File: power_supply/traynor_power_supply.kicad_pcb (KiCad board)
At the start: 2 copper layers, 117 x 47.5 mm, 34 parts, among them J1 AC IN, J10 OUT2, J11 OUT3, J2 AC IN, J3 Chassis GND, J4 OUT1, J5 TREM, J6 SW, J7 SW, J8 CHOKE, J9 CHOKE

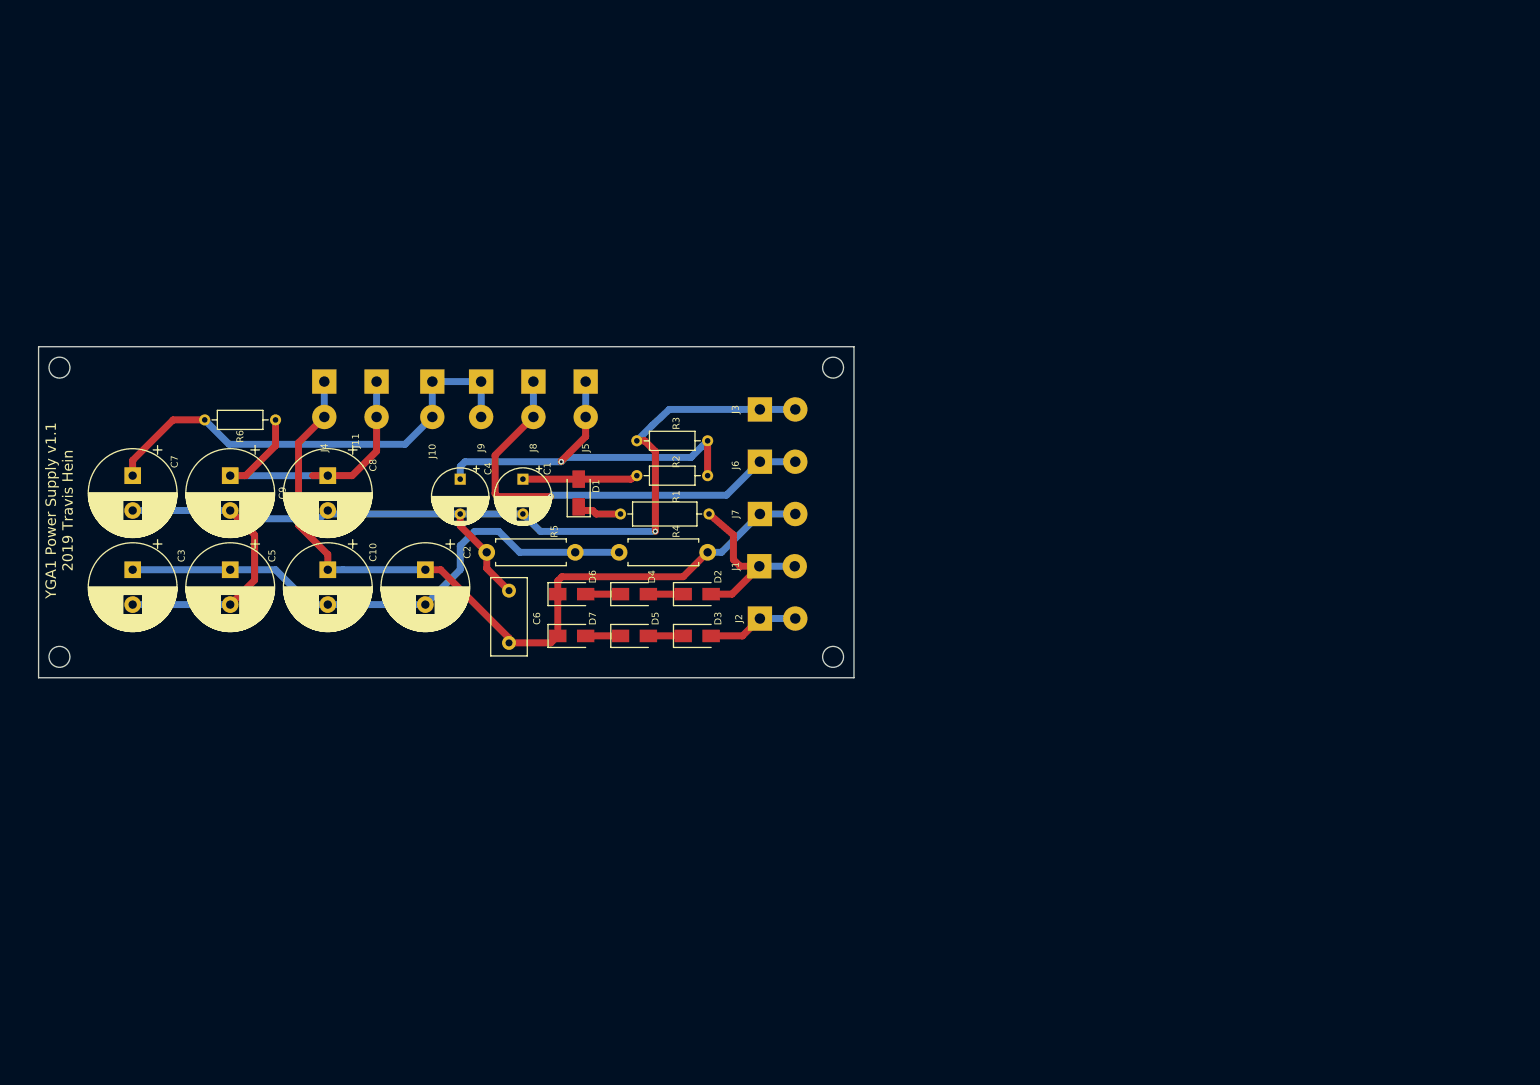
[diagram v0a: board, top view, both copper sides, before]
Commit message: power supply module
assemble circuit board after it arrived.
update schematic to fix bugs and small improvements we observed while wiring it up.
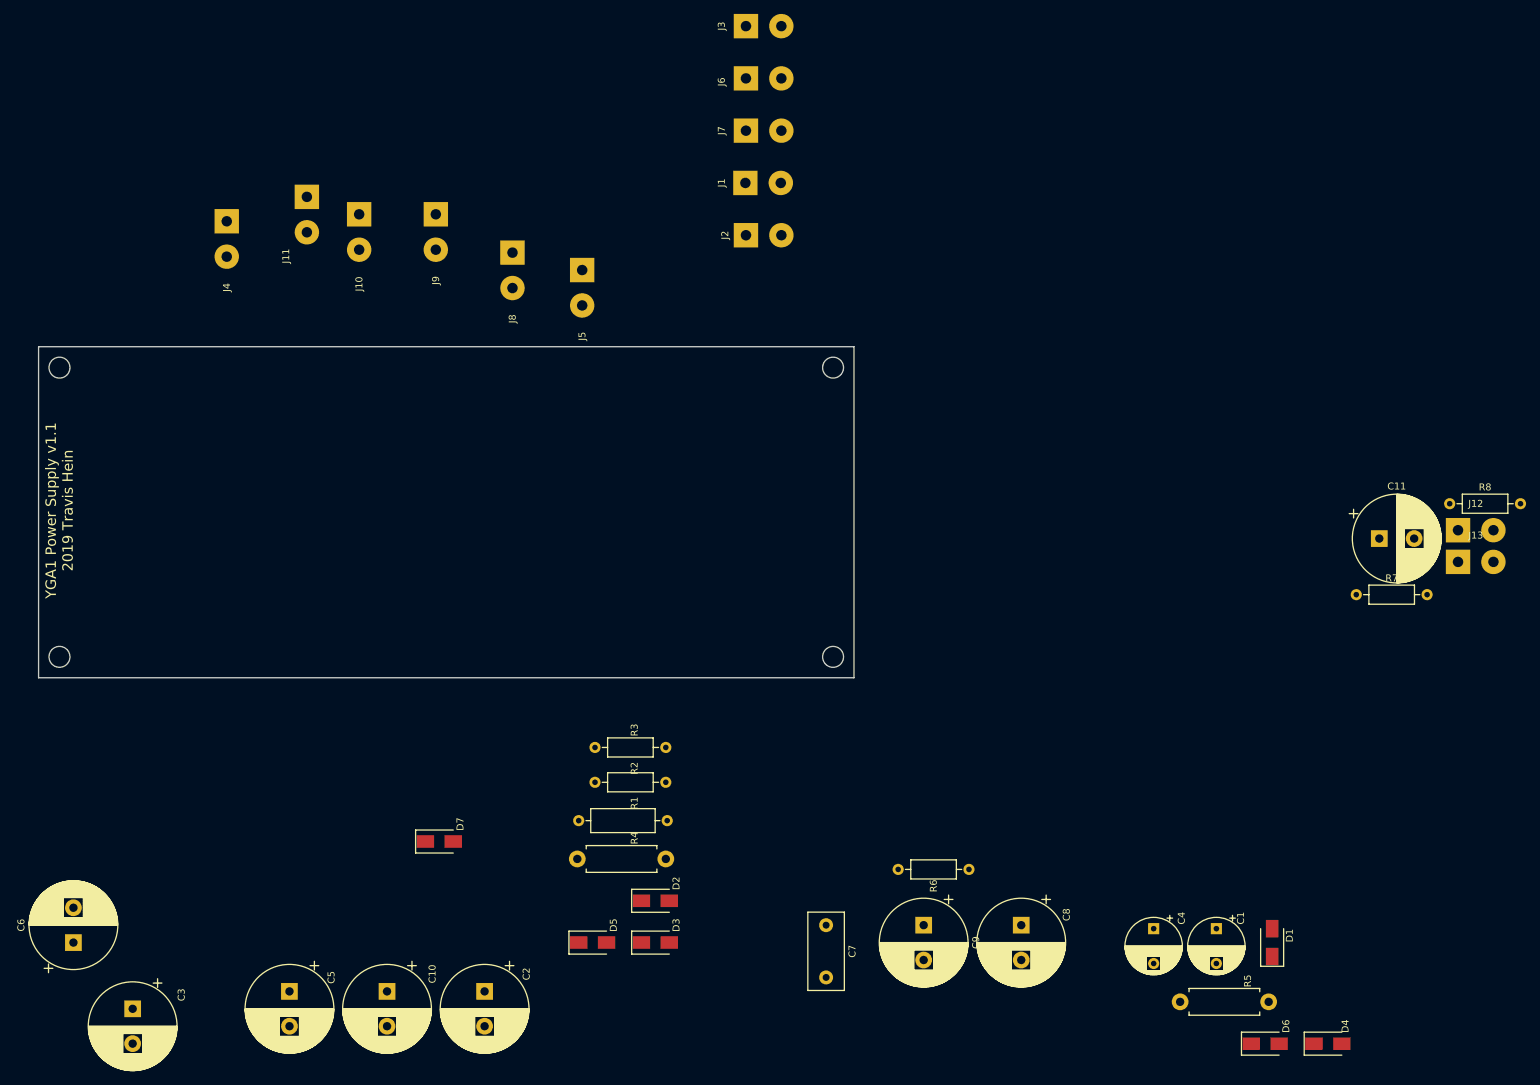
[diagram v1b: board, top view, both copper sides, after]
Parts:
- added C11: 47uF 450V, Capacitor_THT:CP_Radial_D12.5mm_P5.00mm, F.Cu at (242.4, 110.0)
- added J12: +340V, Connector_Wire:SolderWirePad_1x02_P5.08mm_Drill1.5mm, F.Cu at (253.7, 108.8)
- added J13: +340V, Connector_Wire:SolderWirePad_1x02_P5.08mm_Drill1.5mm, F.Cu at (253.7, 113.4)
- added R7: 4.70 1W, Resistor_THT:R_Axial_DIN0207_L6.3mm_D2.5mm_P10.16mm_Horizontal, F.Cu at (239.1, 118.1)
- added R8: 4.7K 1W, Resistor_THT:R_Axial_DIN0207_L6.3mm_D2.5mm_P10.16mm_Horizontal, F.Cu at (252.5, 105.0)
- C6: value 0.047uF 600V -> 47uF 450V; footprint Capacitor_THT:C_Disc_D11.0mm_W5.0mm_P7.50mm -> Capacitor_THT:CP_Radial_D12.5mm_P5.00mm
- C7: value 47uF 450V -> 0.047uF 600V; footprint Capacitor_THT:CP_Radial_D12.5mm_P5.00mm -> Capacitor_THT:C_Disc_D11.0mm_W5.0mm_P7.50mm
- C9: value 10uF 450V -> 47uF 450V
- J10: value OUT2 -> +340V
- J11: value OUT3 -> +340V
- J4: value OUT1 -> -40V
- J5: value TREM -> SW
- J6: value SW -> CHOKE
- J7: value SW -> Audio_center_tap
- J8, J9: value CHOKE -> Output tube
- R6: value 4.7K 1W -> 4.70 1W
- moved C1 118.6 mm to (219.0, 166.0)
- moved C4 118.6 mm to (210.0, 166.0)
- moved C7 118.6 mm to (163.0, 165.5)
- moved C8 118.6 mm to (191.0, 165.5)
- moved C9 118.6 mm to (177.0, 165.5)
- moved D1 118.6 mm to (227.0, 168.0)
- moved D4 118.6 mm to (235.0, 182.5)
- moved D6 118.6 mm to (226.0, 182.5)
- moved R5 118.6 mm to (226.5, 176.5)
- moved R6 118.6 mm to (183.5, 157.5)
- moved C6 75.9 mm to (55.0, 168.0)
- moved C3 63.0 mm to (63.5, 177.5)
- moved C10 61.1 mm to (100.0, 175.0)
- moved C2 61.1 mm to (114.0, 175.0)
- moved C5 61.1 mm to (86.0, 175.0)
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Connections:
- C10 pad 2: Net-(C10-Pad2) -> Net-(C1-Pad1)
- C2 pad 1: Net-(C10-Pad1) -> Net-(C2-Pad1)
- C2 pad 2: Net-(C10-Pad2) -> Net-(C2-Pad2)
- C3 pad 1: Net-(C10-Pad2) -> Net-(C2-Pad2)
- C3 pad 2: Net-(C1-Pad2) -> Net-(C1-Pad1)
- C4 pad 1: Net-(C4-Pad1) -> Net-(C1-Pad1)
- C4 pad 2: Net-(C1-Pad2) -> Net-(C4-Pad2)
- C5 pad 1: Net-(C10-Pad2) -> Net-(C2-Pad1)
- C5 pad 2: Net-(C1-Pad2) -> Net-(C2-Pad2)
- C6 pad 1: Net-(C10-Pad1) -> Net-(C2-Pad2)
- C6 pad 2: Net-(C1-Pad2) -> Net-(C1-Pad1)
- C7 pad 1: Net-(C7-Pad1) -> Net-(C2-Pad1)
- C7 pad 2: Net-(C1-Pad2) -> Net-(C1-Pad1)
- C8 pad 2: Net-(C1-Pad2) -> Net-(C1-Pad1)
- C9 pad 2: Net-(C1-Pad2) -> Net-(C1-Pad1)
- D1 pad 2: Net-(C1-Pad1) -> Net-(C1-Pad2)
- D6 pad 1: Net-(C10-Pad1) -> Net-(C2-Pad1)
- D7 pad 1: Net-(C10-Pad1) -> Net-(C2-Pad1)
- J10 pad 1: Net-(C7-Pad1) -> Net-(C10-Pad1)
- J10 pad 2: Net-(C7-Pad1) -> Net-(C10-Pad1)
- J11 pad 1: Net-(C8-Pad1) -> Net-(C10-Pad1)
- J11 pad 2: Net-(C8-Pad1) -> Net-(C10-Pad1)
- J3 pad 1: Net-(C1-Pad2) -> Net-(C1-Pad1)
- J3 pad 2: Net-(C1-Pad2) -> Net-(C1-Pad1)
- J4 pad 1: Net-(C10-Pad1) -> Net-(C4-Pad2)
- J4 pad 2: Net-(C10-Pad1) -> Net-(C4-Pad2)
- J5 pad 1: Net-(C4-Pad1) -> Net-(C2-Pad1)
- J5 pad 2: Net-(C4-Pad1) -> Net-(C2-Pad1)
- J6 pad 1: Net-(J6-Pad1) -> Net-(C8-Pad1)
- J6 pad 2: Net-(J6-Pad1) -> Net-(C8-Pad1)
- J7 pad 1: Net-(C10-Pad1) -> Net-(C8-Pad1)
- J7 pad 2: Net-(C10-Pad1) -> Net-(C8-Pad1)
- J8 pad 1: Net-(J6-Pad1) -> Net-(J8-Pad1)
- J8 pad 2: Net-(J6-Pad1) -> Net-(J8-Pad1)
- J9 pad 1: Net-(C7-Pad1) -> Net-(J9-Pad1)
- J9 pad 2: Net-(C7-Pad1) -> Net-(J9-Pad1)
- R2 pad 1: Net-(C4-Pad1) -> Net-(C4-Pad2)
- R2 pad 2: Net-(C1-Pad1) -> Net-(C1-Pad2)
- R3 pad 1: Net-(C4-Pad1) -> Net-(C4-Pad2)
- R3 pad 2: Net-(C1-Pad2) -> Net-(C1-Pad1)
- R4 pad 1: Net-(C10-Pad1) -> Net-(C2-Pad1)
- R4 pad 2: Net-(C10-Pad2) -> Net-(C2-Pad2)
- R5 pad 1: Net-(C10-Pad2) -> Net-(C2-Pad2)
- R5 pad 2: Net-(C1-Pad2) -> Net-(C1-Pad1)
- R6 pad 1: Net-(C8-Pad1) -> Net-(J8-Pad1)
- R6 pad 2: Net-(C7-Pad1) -> Net-(C8-Pad1)
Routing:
- net Net-(C1-Pad2): track 160.9 -> 0.00 mm, vias 1 -> 0
- net Net-(C10-Pad1): track 114.4 -> 0.00 mm
- net Net-(C10-Pad2): track 79.5 -> 0.00 mm
- net Net-(C7-Pad1): track 67.8 -> 0.00 mm
- net Net-(J6-Pad1): track 63.7 -> 0.00 mm, vias 1 -> 0
- net Net-(C4-Pad1): track 56.3 -> 0.00 mm, vias 1 -> 0
- net Net-(C8-Pad1): track 46.6 -> 0.00 mm
- net Net-(D2-Pad2): track 26.0 -> 0.00 mm
- net Net-(C1-Pad1): track 16.5 -> 0.00 mm
- net Net-(D3-Pad2): track 13.1 -> 0.00 mm
- net Net-(D1-Pad1): track 6.41 -> 0.00 mm
- net Net-(D5-Pad1): track 5.00 -> 0.00 mm
- net Net-(D4-Pad1): track 5.00 -> 0.00 mm
- net Net-(D3-Pad1): track 5.00 -> 0.00 mm
- net Net-(D2-Pad1): track 5.00 -> 0.00 mm
